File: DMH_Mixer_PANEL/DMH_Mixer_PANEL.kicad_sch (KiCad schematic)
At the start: 5 parts, among them J0 Panel_GND_Solder_Wire_Pad

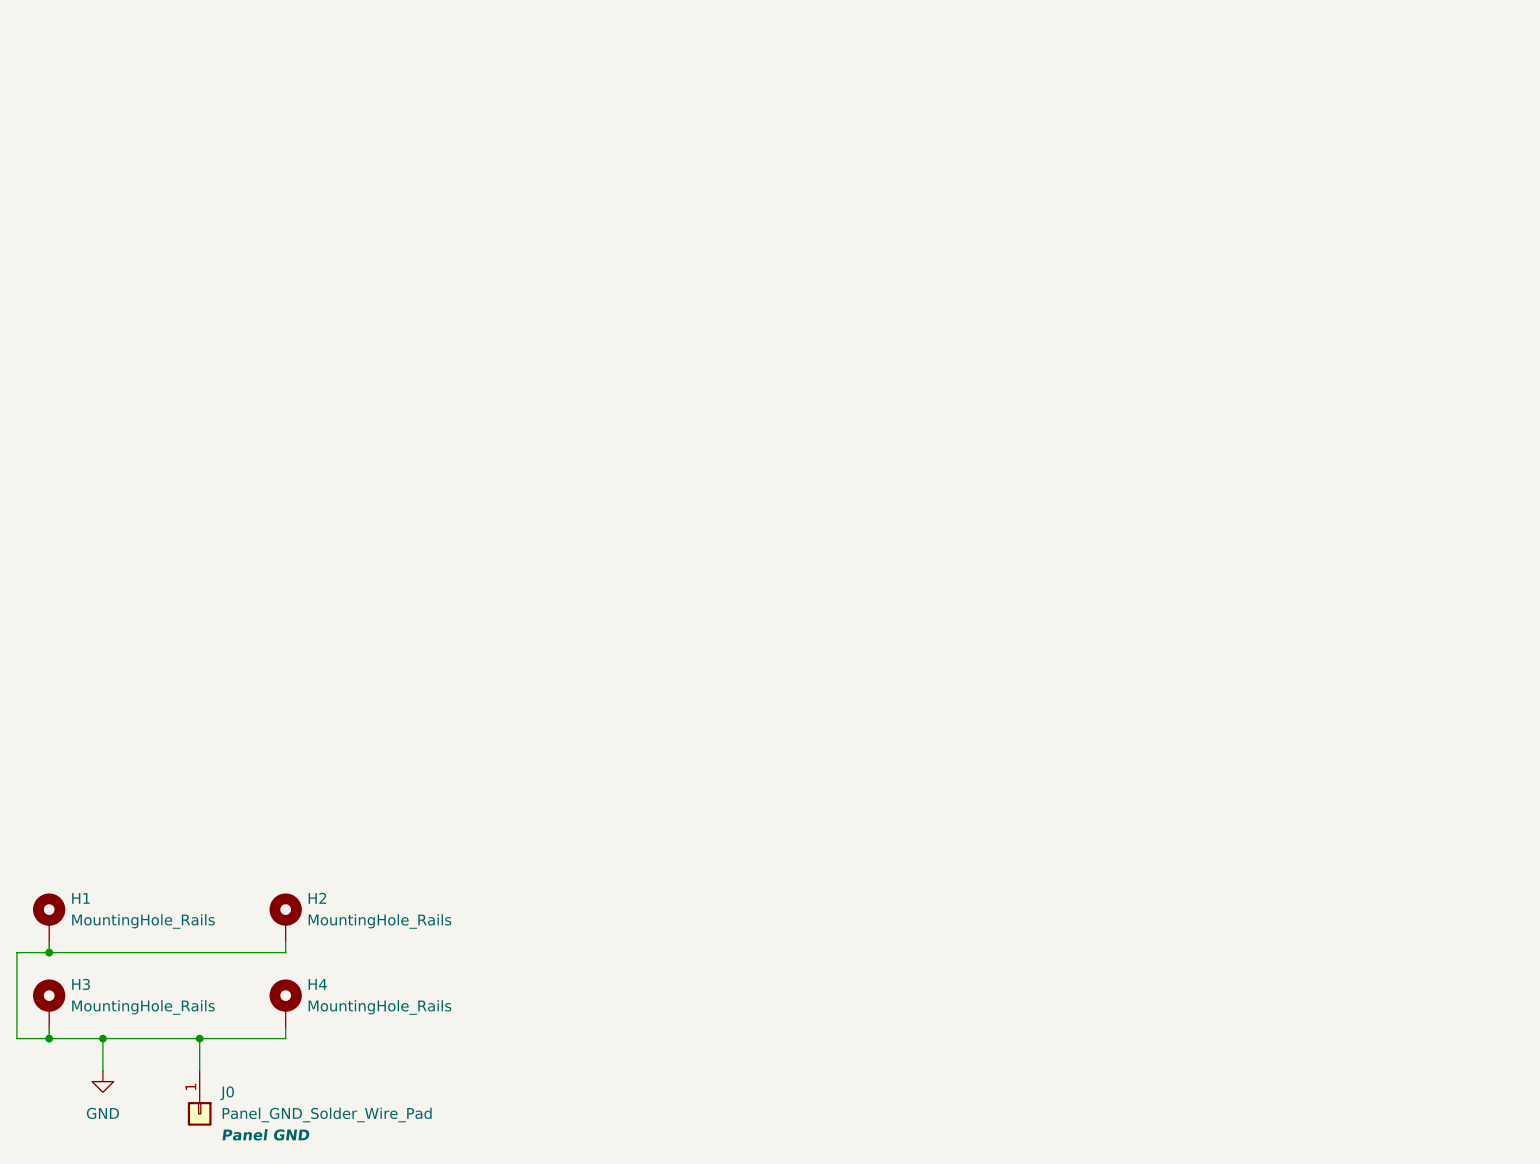
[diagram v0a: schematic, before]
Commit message: Designed mixer front panel
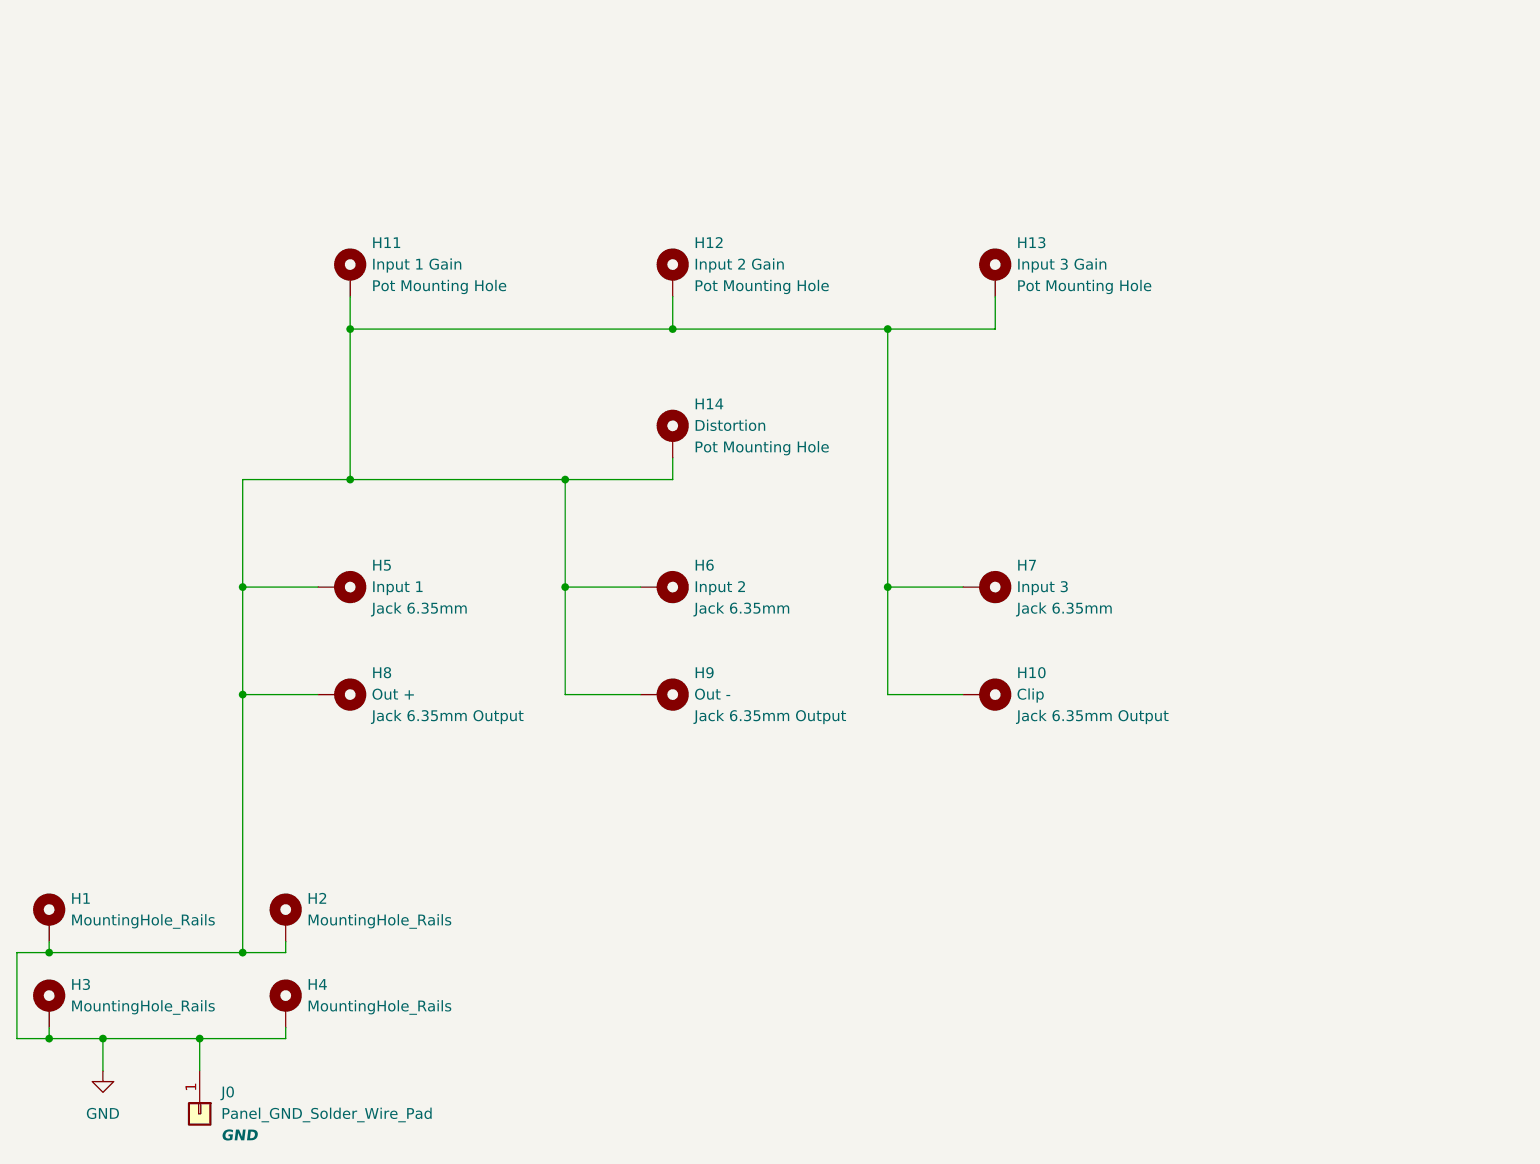
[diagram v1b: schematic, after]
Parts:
- added H10: Clip, SynthStuff:Jack_6.35mm_Cutout_Output_v6, symbol SynthStuff:MountingHole_Jack6.35mm_Output_v2
- added H11: Input 1 Gain, SynthStuff:Pot_Cutout_Small, symbol SynthStuff:MountingHole_Pot
- added H12: Input 2 Gain, SynthStuff:Pot_Cutout_Small, symbol SynthStuff:MountingHole_Pot
- added H13: Input 3 Gain, SynthStuff:Pot_Cutout_Small, symbol SynthStuff:MountingHole_Pot
- added H14: Distortion, SynthStuff:Pot_Cutout_Tiny, symbol SynthStuff:MountingHole_Pot
- added H5: Input 1, SynthStuff:Jack_6.35mm_Cutout_v3, symbol SynthStuff:MountingHole_Jack6.35mm_v2
- added H6: Input 2, SynthStuff:Jack_6.35mm_Cutout_v3, symbol SynthStuff:MountingHole_Jack6.35mm_v2
- added H7: Input 3, SynthStuff:Jack_6.35mm_Cutout_v3, symbol SynthStuff:MountingHole_Jack6.35mm_v2
- added H8: Out +, SynthStuff:Jack_6.35mm_Cutout_Output_v6, symbol SynthStuff:MountingHole_Jack6.35mm_Output_v2
- added H9: Out -, SynthStuff:Jack_6.35mm_Cutout_Output_v6, symbol SynthStuff:MountingHole_Jack6.35mm_Output_v2
- J0: Function Panel GND -> GND
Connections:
- net GND: now also H10.1, H11.1, H12.1, H13.1, H14.1, H5.1, H6.1, H7.1, H8.1, H9.1

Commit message: Replaced clipping with 4th channel on panel
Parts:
- removed H10: Clip, SynthStuff:Jack_6.35mm_Cutout_Output_v6, symbol SynthStuff:MountingHole_Jack6.35mm_Output_v2
- removed H14: Distortion, SynthStuff:Pot_Cutout_Tiny, symbol SynthStuff:MountingHole_Pot
- added H15: Input 4, SynthStuff:Jack_6.35mm_Cutout_v3, symbol SynthStuff:MountingHole_Jack6.35mm_v2
- added H16: Input 4 Gain, SynthStuff:Pot_Cutout_Small, symbol SynthStuff:MountingHole_Pot
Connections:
- net GND: now also H15.1, H16.1
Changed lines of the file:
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@@
+	)
+	(junction
+		(at 139.7 185.42)
+		(diameter 0)
+		(color 0 0 0 0)
 	)
 	(junction
@@
 	)
 	(junction
+		(at 127 203.2)
+		(diameter 0)
+		(color 0 0 0 0)
+	)
+	(junction
 		(at 101.6 185.42)
 		(diameter 0)
@@
 	)
 	(junction
-		(at 88.9 203.2)
-		(diameter 0)
-		(color 0 0 0 0)
-	)
-	(junction
-		(at 127 215.9)
-		(diameter 0)
-		(color 0 0 0 0)
-	)
-	(junction
 		(at 50.8 259.08)
 		(diameter 0)
@@
 	(wire
 		(pts
-			(xy 127 228.6) (xy 127 215.9)
-		)
-		(stroke
-			(width 0)
-			(type default)
-		)
-	)
-	(wire
-		(pts
 			(xy 127 185.42) (xy 101.6 185.42)
 		)
@@
 	(wire
 		(pts
-			(xy 135.89 228.6) (xy 127 228.6)
+			(xy 139.7 185.42) (xy 165.1 185.42)
 		)
 		(stroke
@@
 	(wire
 		(pts
+			(xy 161.29 215.9) (xy 157.48 215.9)
+		)
+		(stroke
+			(width 0)
+			(type default)
+		)
+	)
+	(wire
+		(pts
 			(xy 50.8 259.08) (xy 55.88 259.08)
 		)
@@
 	(wire
 		(pts
-			(xy 101.6 200.66) (xy 101.6 203.2)
+			(xy 127 203.2) (xy 157.48 203.2)
 		)
 		(stroke
@@
 	(wire
 		(pts
+			(xy 127 203.2) (xy 127 185.42)
+		)
+		(stroke
+			(width 0)
+			(type default)
+		)
+	)
+	(wire
+		(pts
 			(xy 88.9 228.6) (xy 88.9 215.9)
 		)
@@
 	(wire
 		(pts
-			(xy 88.9 203.2) (xy 101.6 203.2)
-		)
-		(stroke
-			(width 0)
-			(type default)
-		)
-	)
-	(wire
-		(pts
 			(xy 63.5 203.2) (xy 88.9 203.2)
 		)
@@
 	(wire
 		(pts
-			(xy 127 215.9) (xy 127 185.42)
+			(xy 157.48 215.9) (xy 157.48 203.2)
+		)
+		(stroke
+			(width 0)
+			(type default)
+		)
+	)
+	(wire
+		(pts
+			(xy 127 215.9) (xy 127 203.2)
+		)
+		(stroke
+			(width 0)
+			(type default)
+		)
+	)
+	(wire
+		(pts
+			(xy 165.1 181.61) (xy 165.1 185.42)
 		)
 		(stroke
@@
 	)
 	(symbol
+		(lib_id "SynthStuff:MountingHole_Pot")
+		(at 165.1 179.07 0)
+		(unit 1)
+		(exclude_from_sim yes)
+		(in_bom no)
+		(on_board yes)
+		(dnp no)
+		(fields_autoplaced yes)
+		(property "Reference" "H16"
+			(at 167.64 175.2599 0)
+			(effects
+				(font
+					(size 1.27 1.27)
+				)
+				(justify left)
+			)
+		)
+		(property "Value" "Input 4 Gain"
+			(at 167.64 177.7999 0)
+			(effects
+				(font
+					(size 1.27 1.27)
+				)
+				(justify left)
+			)
+		)
+		(property "Footprint" "SynthStuff:Pot_Cutout_Small"
+			(at 165.1 179.07 0)
+			(effects
+				(font
+					(size 1.27 1.27)
+				)
+				(hide yes)
+			)
+		)
+		(property "Datasheet" "~"
+			(at 165.1 179.07 0)
+			(effects
+				(font
+					(size 1.27 1.27)
+				)
+				(hide yes)
+			)
+		)
+		(property "Description" "Pot Mounting Hole"
+			(at 167.64 180.3399 0)
+			(effects
+				(font
+					(size 1.27 1.27)
+				)
+				(justify left)
+			)
+		)
+		(pin "1"
+		)
+		(instances
+			(project "DMH_Mixer_PANEL"
+				(path "/a552705f-a9fe-462e-9913-5cfcc08b233c"
+					(reference "H16")
+					(unit 1)
+				)
+			)
+		)
+	)
+	(symbol
 		(lib_id "SynthStuff:MountingHole_Jack6.35mm_v2")
 		(at 139.7 215.9 0)
@@
 				(path "/a552705f-a9fe-462e-9913-5cfcc08b233c"
 					(reference "H7")
+					(unit 1)
+				)
+			)
+		)
+	)
+	(symbol
+		(lib_id "SynthStuff:MountingHole_Jack6.35mm_v2")
+		(at 165.1 215.9 0)
+		(unit 1)
+		(exclude_from_sim yes)
+		(in_bom no)
+		(on_board yes)
+		(dnp no)
+		(fields_autoplaced yes)
+		(property "Reference" "H15"
+			(at 167.64 213.3599 0)
+			(effects
+				(font
+					(size 1.27 1.27)
+				)
+				(justify left)
+			)
+		)
+		(property "Value" "Input 4"
+			(at 167.64 215.8999 0)
+			(effects
+				(font
+					(size 1.27 1.27)
+				)
+				(justify left)
+			)
+		)
+		(property "Footprint" "SynthStuff:Jack_6.35mm_Cutout_v3"
+			(at 165.1 215.9 0)
+			(effects
+				(font
+					(size 1.27 1.27)
+				)
+				(hide yes)
+			)
+		)
+		(property "Datasheet" "~"
+			(at 165.1 215.9 0)
+			(effects
+				(font
+					(size 1.27 1.27)
+				)
+				(hide yes)
+			)
+		)
+		(property "Description" "Jack 6.35mm"
+			(at 167.64 218.4399 0)
+			(effects
+				(font
+					(size 1.27 1.27)
+				)
+				(justify left)
+			)
+		)
+		(pin "1"
+		)
+		(instances
+			(project "DMH_Mixer_PANEL"
+				(path "/a552705f-a9fe-462e-9913-5cfcc08b233c"
+					(reference "H15")
 					(unit 1)
 				)
@@
 					(unit 1)
 				)
-			)
-		)
-	)
-	(symbol
-		(lib_id "SynthStuff:MountingHole_Pot")
-		(at 101.6 198.12 0)
-		(unit 1)
-		(exclude_from_sim yes)
-		(in_bom no)
-		(on_board yes)
-		(dnp no)
-		(fields_autoplaced yes)
-		(property "Reference" "H14"
-			(at 104.14 194.3099 0)
-			(effects
-				(font
-					(size 1.27 1.27)
-				)
-				(justify left)
-			)
-		)
-		(property "Value" "Distortion"
-			(at 104.14 196.8499 0)
-			(effects
-				(font
-					(size 1.27 1.27)
-				)
-				(justify left)
-			)
-		)
-		(property "Footprint" "SynthStuff:Pot_Cutout_Tiny"
-			(at 101.6 198.12 0)
-			(effects
-				(font
-					(size 1.27 1.27)
-				)
-				(hide yes)
-			)
-		)
-		(property "Datasheet" "~"
-			(at 101.6 198.12 0)
-			(effects
-				(font
-					(size 1.27 1.27)
-				)
-				(hide yes)
-			)
-		)
-		(property "Description" "Pot Mounting Hole"
-			(at 104.14 199.3899 0)
-			(effects
-				(font
-					(size 1.27 1.27)
-				)
-				(justify left)
-			)
-		)
-		(pin "1"
-		)
-		(instances
-			(project ""
-				(path "/a552705f-a9fe-462e-9913-5cfcc08b233c"
-					(reference "H14")
-					(unit 1)
-				)
-			)
-		)
-	)
-	(symbol
-		(lib_id "SynthStuff:MountingHole_Jack6.35mm_Output_v2")
-		(at 139.7 228.6 0)
-		(unit 1)
-		(exclude_from_sim yes)
-		(in_bom no)
-		(on_board yes)
-		(dnp no)
-		(fields_autoplaced yes)
-		(property "Reference" "H10"
-			(at 142.24 226.0599 0)
-			(effects
-				(font
-					(size 1.27 1.27)
-				)
-				(justify left)
-			)
-		)
-		(property "Value" "Clip"
-			(at 142.24 228.5999 0)
-			(effects
-				(font
-					(size 1.27 1.27)
-				)
-				(justify left)
-			)
-		)
-		(property "Footprint" "SynthStuff:Jack_6.35mm_Cutout_Output_v6"
-			(at 139.7 228.6 0)
-			(effects
-				(font
-					(size 1.27 1.27)
-				)
-				(hide yes)
-			)
-		)
-		(property "Datasheet" "~"
-			(at 139.7 228.6 0)
-			(effects
-				(font
-					(size 1.27 1.27)
-				)
-				(hide yes)
-			)
-		)
-		(property "Description" "Jack 6.35mm Output"
-			(at 142.24 231.1399 0)
-			(effects
-				(font
-					(size 1.27 1.27)
-				)
-				(justify left)
-			)
-		)
-		(pin "1"
-		)
-		(instances
-			(project ""
-				(path "/a552705f-a9fe-462e-9913-5cfcc08b233c"
-					(reference "H10")
-					(unit 1)
-				)

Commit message: Added 4th channel to schematic
... and replaced Inverted Output with Clipped Output
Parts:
- H15: value Input 4 -> In 4
- H5: value Input 1 -> In 1
- H6: value Input 2 -> In 2
- H7: value Input 3 -> In 3
- H8: value Out + -> Out
- H9: value Out - -> Clip
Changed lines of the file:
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@@
 			)
 		)
-		(property "Value" "Out +"
+		(property "Value" "Out"
 			(at 66.04 228.5999 0)
 			(effects
@@
 			)
 		)
-		(property "Value" "Out -"
+		(property "Value" "Clip"
 			(at 104.14 228.5999 0)
 			(effects
@@
 			)
 		)
-		(property "Value" "Input 3"
+		(property "Value" "In 3"
 			(at 142.24 215.8999 0)
 			(effects
@@
 			)
 		)
-		(property "Value" "Input 4"
+		(property "Value" "In 4"
 			(at 167.64 215.8999 0)
 			(effects
@@
 			)
 		)
-		(property "Value" "Input 1"
+		(property "Value" "In 1"
 			(at 66.04 215.8999 0)
 			(effects
@@
 			)
 		)
-		(property "Value" "Input 2"
+		(property "Value" "In 2"
 			(at 104.14 215.8999 0)
 			(effects

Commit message: PCB redesign in progress
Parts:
- added H10: Clip Amt, SynthStuff:MountingHole_TrimPot, symbol SynthStuff:MountingHole_Trimpot
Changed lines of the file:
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@@
+	)
+	(symbol
+		(lib_id "SynthStuff:MountingHole_Trimpot")
+		(at 139.7 165.1 0)
+		(unit 1)
+		(exclude_from_sim yes)
+		(in_bom no)
+		(on_board yes)
+		(dnp no)
+		(fields_autoplaced yes)
+		(property "Reference" "H10"
+			(at 142.24 162.5599 0)
+			(effects
+				(font
+					(size 1.27 1.27)
+				)
+				(justify left)
+			)
+		)
+		(property "Value" "Clip Amt"
+			(at 142.24 165.0999 0)
+			(effects
+				(font
+					(size 1.27 1.27)
+				)
+				(justify left)
+			)
+		)
+		(property "Footprint" "SynthStuff:MountingHole_TrimPot"
+			(at 139.7 165.1 0)
+			(effects
+				(font
+					(size 1.27 1.27)
+				)
+				(hide yes)
+			)
+		)
+		(property "Datasheet" "~"
+			(at 139.7 165.1 0)
+			(effects
+				(font
+					(size 1.27 1.27)
+				)
+				(hide yes)
+			)
+		)
+		(property "Description" "Mounting Hole Trimpot"
+			(at 142.24 167.6399 0)
+			(effects
+				(font
+					(size 1.27 1.27)
+				)
+				(justify left)
+			)
+		)
+		(instances
+			(project ""
+				(path "/a552705f-a9fe-462e-9913-5cfcc08b233c"
+					(reference "H10")
+					(unit 1)
+				)
+			)
+		)
 	)
 	(symbol

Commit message: Added toggle switches to front panel
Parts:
- added H14: Input 1 Line/10Vpp, SynthStuff:Toggle_Switch_Cutout, symbol SynthStuff:MountingHole_ToggleSwitch
- added H17: Input 2 Line/10Vpp, SynthStuff:Toggle_Switch_Cutout, symbol SynthStuff:MountingHole_ToggleSwitch
- added H18: Input 3 Line/10Vpp, SynthStuff:Toggle_Switch_Cutout, symbol SynthStuff:MountingHole_ToggleSwitch
- added H19: Input 4 Line/10Vpp, SynthStuff:Toggle_Switch_Cutout, symbol SynthStuff:MountingHole_ToggleSwitch
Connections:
- net GND: now also H14.1, H17.1, H18.1, H19.1
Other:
- moved on the sheet: H16

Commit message: Finalization in progress
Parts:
- removed H10: Clip Amt, SynthStuff:MountingHole_TrimPot, symbol SynthStuff:MountingHole_Trimpot
- removed H9: Clip, SynthStuff:Jack_6.35mm_Cutout_Output_v6, symbol SynthStuff:MountingHole_Jack6.35mm_Output_v2
- added H9: Clip, SynthStuff:Toggle_Switch_Cutout, symbol SynthStuff:MountingHole_ToggleSwitch
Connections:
- net GND: now also H9.1
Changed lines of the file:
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@@
+	)
+	(symbol
+		(lib_id "SynthStuff:MountingHole_ToggleSwitch")
+		(at 101.6 228.6 270)
+		(unit 1)
+		(exclude_from_sim yes)
+		(in_bom no)
+		(on_board yes)
+		(dnp no)
+		(fields_autoplaced yes)
+		(property "Reference" "H9"
+			(at 104.14 226.0599 90)
+			(effects
+				(font
+					(size 1.27 1.27)
+				)
+				(justify left)
+			)
+		)
+		(property "Value" "Clip"
+			(at 104.14 228.5999 90)
+			(effects
+				(font
+					(size 1.27 1.27)
+				)
+				(justify left)
+			)
+		)
+		(property "Footprint" "SynthStuff:Toggle_Switch_Cutout"
+			(at 101.6 228.6 0)
+			(effects
+				(font
+					(size 1.27 1.27)
+				)
+				(hide yes)
+			)
+		)
+		(property "Datasheet" "~"
+			(at 101.6 228.6 0)
+			(effects
+				(font
+					(size 1.27 1.27)
+				)
+				(hide yes)
+			)
+		)
+		(property "Description" "Toggle Switch Mounting Hole"
+			(at 104.14 231.1399 90)
+			(effects
+				(font
+					(size 1.27 1.27)
+				)
+				(justify left)
+			)
+		)
+		(pin "1"
+		)
+		(instances
+			(project "DMH_Mixer_PANEL"
+				(path "/a552705f-a9fe-462e-9913-5cfcc08b233c"
+					(reference "H9")
+					(unit 1)
+				)
+			)
+		)
 	)
 	(symbol
@@
 					(unit 1)
 				)
-			)
-		)
-	)
-	(symbol
-		(lib_id "SynthStuff:MountingHole_Jack6.35mm_Output_v2")
-		(at 101.6 228.6 0)
-		(unit 1)
-		(exclude_from_sim yes)
-		(in_bom no)
-		(on_board yes)
-		(dnp no)
-		(fields_autoplaced yes)
-		(property "Reference" "H9"
-			(at 104.14 226.0599 0)
-			(effects
-				(font
-					(size 1.27 1.27)
-				)
-				(justify left)
-			)
-		)
-		(property "Value" "Clip"
-			(at 104.14 228.5999 0)
-			(effects
-				(font
-					(size 1.27 1.27)
-				)
-				(justify left)
-			)
-		)
-		(property "Footprint" "SynthStuff:Jack_6.35mm_Cutout_Output_v6"
-			(at 101.6 228.6 0)
-			(effects
-				(font
-					(size 1.27 1.27)
-				)
-				(hide yes)
-			)
-		)
-		(property "Datasheet" "~"
-			(at 101.6 228.6 0)
-			(effects
-				(font
-					(size 1.27 1.27)
-				)
-				(hide yes)
-			)
-		)
-		(property "Description" "Jack 6.35mm Output"
-			(at 104.14 231.1399 0)
-			(effects
-				(font
-					(size 1.27 1.27)
-				)
-				(justify left)
-			)
-		)
-		(pin "1"
-		)
-		(instances
-			(project ""
-				(path "/a552705f-a9fe-462e-9913-5cfcc08b233c"
-					(reference "H9")
-					(unit 1)
-				)
-			)
-		)
-	)
-	(symbol
-		(lib_id "SynthStuff:MountingHole_Trimpot")
-		(at 139.7 165.1 0)
-		(unit 1)
-		(exclude_from_sim yes)
-		(in_bom no)
-		(on_board yes)
-		(dnp no)
-		(fields_autoplaced yes)
-		(property "Reference" "H10"
-			(at 142.24 162.5599 0)
-			(effects
-				(font
-					(size 1.27 1.27)
-				)
-				(justify left)
-			)
-		)
-		(property "Value" "Clip Amt"
-			(at 142.24 165.0999 0)
-			(effects
-				(font
-					(size 1.27 1.27)
-				)
-				(justify left)
-			)
-		)
-		(property "Footprint" "SynthStuff:MountingHole_TrimPot"
-			(at 139.7 165.1 0)
-			(effects
-				(font
-					(size 1.27 1.27)
-				)
-				(hide yes)
-			)
-		)
-		(property "Datasheet" "~"
-			(at 139.7 165.1 0)
-			(effects
-				(font
-					(size 1.27 1.27)
-				)
-				(hide yes)
-			)
-		)
-		(property "Description" "Mounting Hole Trimpot"
-			(at 142.24 167.6399 0)
-			(effects
-				(font
-					(size 1.27 1.27)
-				)
-				(justify left)
-			)
-		)
-		(instances
-			(project ""
-				(path "/a552705f-a9fe-462e-9913-5cfcc08b233c"
-					(reference "H10")
-					(unit 1)
-				)

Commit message: Panel and Connectors PCB ready
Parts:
- H9: footprint SynthStuff:Toggle_Switch_Cutout -> SynthStuff:Toggle_Switch_APEM_Cutout
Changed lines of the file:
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@@
 			)
 		)
-		(property "Footprint" "SynthStuff:Toggle_Switch_Cutout"
+		(property "Footprint" "SynthStuff:Toggle_Switch_APEM_Cutout"
 			(at 101.6 228.6 0)
 			(effects

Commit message: Generated BoM
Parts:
- H11, H12, H13, H16: now in the parts list
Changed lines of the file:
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@@
 		(unit 1)
 		(exclude_from_sim yes)
-		(in_bom no)
+		(in_bom yes)
 		(on_board yes)
 		(dnp no)
@@
 		(unit 1)
 		(exclude_from_sim yes)
-		(in_bom no)
+		(in_bom yes)
 		(on_board yes)
 		(dnp no)
@@
 		(unit 1)
 		(exclude_from_sim yes)
-		(in_bom no)
+		(in_bom yes)
 		(on_board yes)
 		(dnp no)
@@
 		(unit 1)
 		(exclude_from_sim yes)
-		(in_bom no)
-		(on_board yes)
-		(dnp no)
+		(in_bom yes)
+		(on_board yes)
+		(dnp no)
